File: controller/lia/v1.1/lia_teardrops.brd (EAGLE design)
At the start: 58.2 x 33.6 mm, 122 parts, among them IC9 LP2992 5V, J1 CONN_3-1, J2 CONN_3-1, J3 CONN_3-1, J4 CONN_3-1, J5 CONN_3-1, J6 CONN_3-1, J7 CONN_3-1, J8 CONN_3-1, Q1 12Mhz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

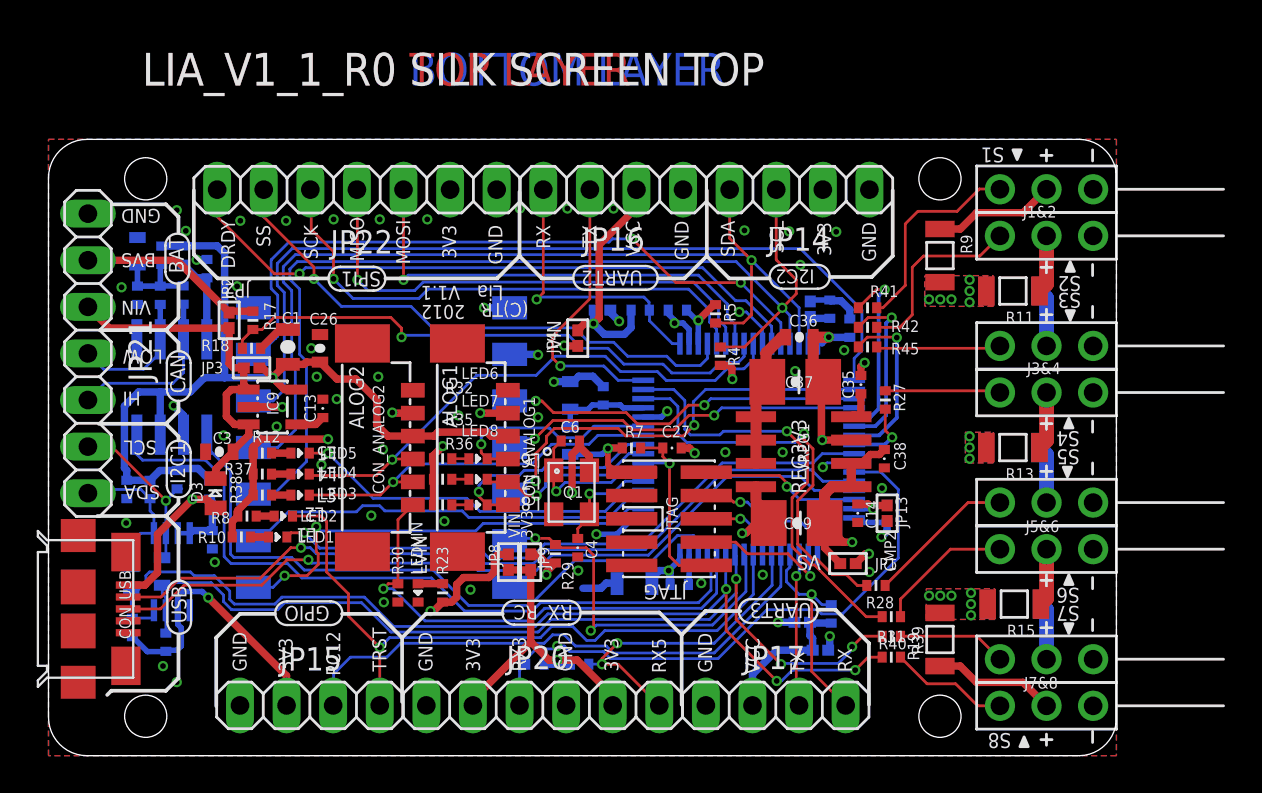
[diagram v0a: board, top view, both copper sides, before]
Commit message: Added gerber generation scripts to lia v1.1.
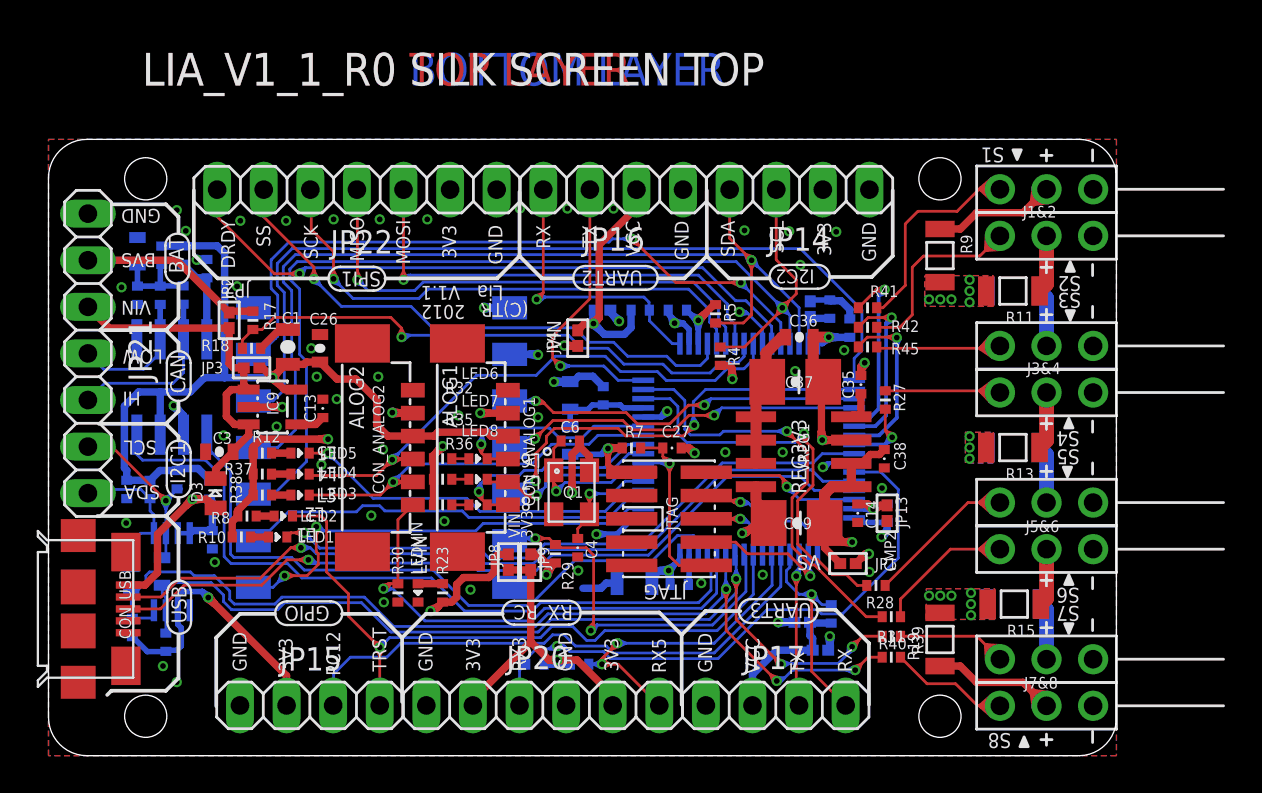
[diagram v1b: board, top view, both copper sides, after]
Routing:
- net +3V3: track 65.6 -> 93.1 mm
- net GND: track 41.1 -> 54.2 mm
- net SERVO_8/I2C1_SDA: track 53.2 -> 61.9 mm
- net SERVO_7/I2C1_SCL: track 50.6 -> 59.3 mm
- net UART5_RX: track 17.7 -> 23.9 mm
- net USB_VBUS: track 62.7 -> 68.2 mm
- net V_IN: track 41.3 -> 46.6 mm
- net IMU_MAG_DRDY: track 20.6 -> 25.6 mm
- net IMU_SPI_MISO: track 19.9 -> 24.8 mm
- net IMU_GYRO_SS: track 24.6 -> 29.6 mm
- net I2C2_SDA: track 52.9 -> 57.8 mm
- net IMU_SPI_MOSI: track 20.1 -> 25.1 mm
- net I2C2_SCL: track 56.2 -> 61.2 mm
- net IMU_SPI_SCK: track 23.4 -> 28.4 mm
- net IMU_ACC_DRDY: track 37.3 -> 42.3 mm
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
